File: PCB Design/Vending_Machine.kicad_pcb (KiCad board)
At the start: 2 copper layers, 113.8 x 144.3 mm, 126 parts, among them J1 Mains, J11 Conn_Sig, J12 Conn_Aux, J13 Conn_I2C, J15 Conn_I2C, J2 Conn_0-7, J3 Conn_8, J31 Conn_01x15, J32 Conn_01x15, J33 UART0, J34 UART2, J35 GPIO, J36 Display, J37 I2C, J38 I2C, J39 SPI, J4 Conn_9, J40 GPIO, SW31 EN, SW32 BOOT, U11 AMS1117-3.3, U12 SX1509BIULTRT, U13 TCA9406DC, U31 AMS1117-3.3, U32 ESP32-WROOM-32UE, U33 TCA9406DC

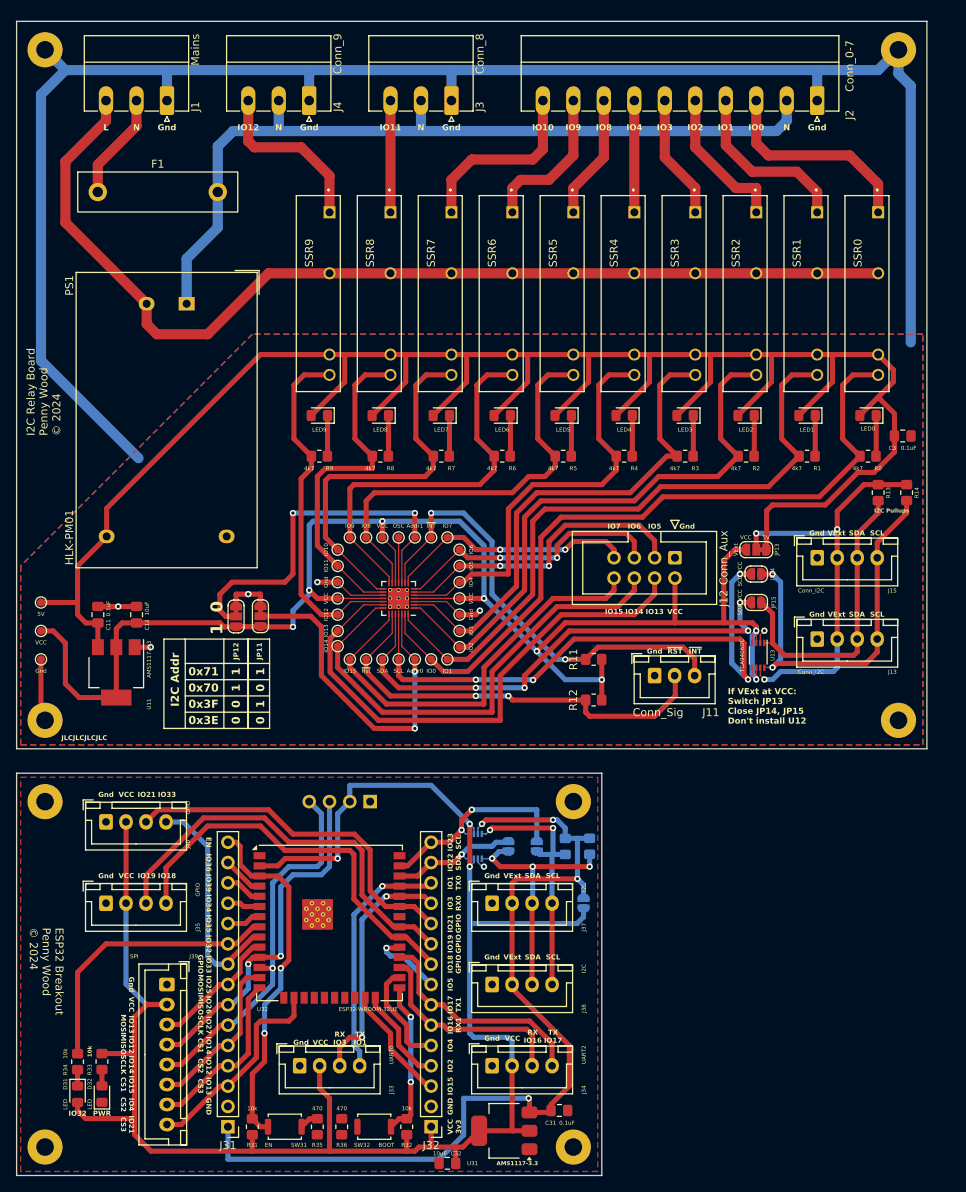
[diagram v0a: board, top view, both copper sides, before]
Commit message: Added Multiplexer
Added separate IO Multiplexer breakout
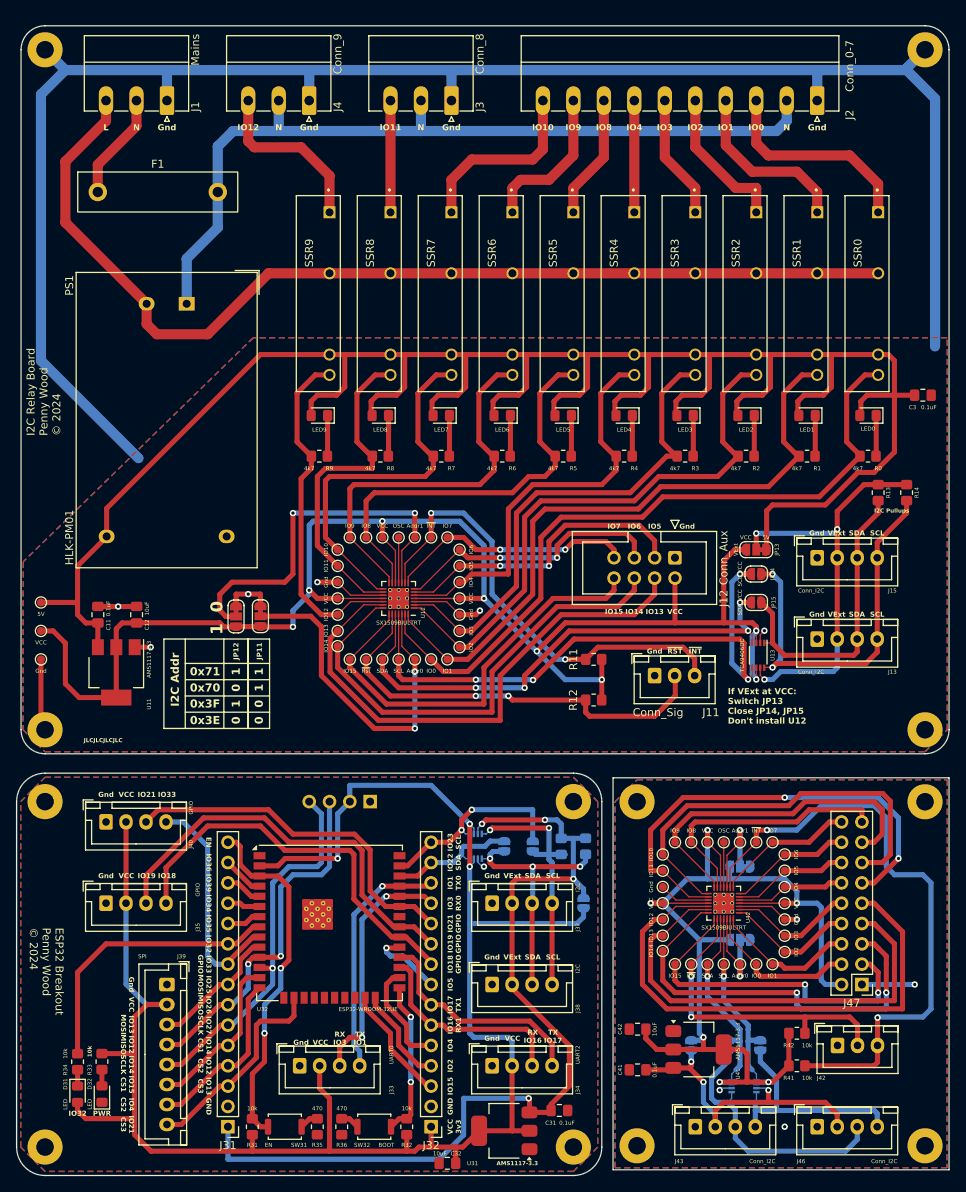
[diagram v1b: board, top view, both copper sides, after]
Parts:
- added Addr0: , Footprints:TestPoint_Pad_D1.0mm, F.Cu at (137.7, 165.1)
- added Addr1: , Footprints:TestPoint_Pad_D1.0mm, F.Cu at (137.7, 149.9)
- added C41: 0.1uF, Capacitor_SMD:C_0805_2012Metric_Pad1.18x1.45mm_HandSolder, F.Cu at (124.9, 178.3)
- added C42: 10uF, Capacitor_SMD:C_0805_2012Metric_Pad1.18x1.45mm_HandSolder, F.Cu at (124.9, 173.2)
- added Gnd: , Footprints:TestPoint_Pad_D1.0mm, F.Cu at (128.0, 155.4)
- added Gnd: , Footprints:TestPoint_Pad_D1.0mm, F.Cu at (143.3, 159.5)
- added H31: MountingHole_2.2mm_M2_Pad, MountingHole:MountingHole_2.2mm_M2_Pad, F.Cu at (160.8, 144.8)
- added H31: MountingHole_2.2mm_M2_Pad, MountingHole:MountingHole_2.2mm_M2_Pad, F.Cu at (124.8, 144.8)
- added H31: MountingHole_2.2mm_M2_Pad, MountingHole:MountingHole_2.2mm_M2_Pad, F.Cu at (160.8, 187.8)
- added H31: MountingHole_2.2mm_M2_Pad, MountingHole:MountingHole_2.2mm_M2_Pad, F.Cu at (124.8, 187.8)
- added IO0: , Footprints:TestPoint_Pad_D1.0mm, F.Cu at (139.7, 165.1)
- added IO1: , Footprints:TestPoint_Pad_D1.0mm, F.Cu at (141.7, 165.1)
- added IO10: , Footprints:TestPoint_Pad_D1.0mm, F.Cu at (128.0, 151.4)
- added IO11: , Footprints:TestPoint_Pad_D1.0mm, F.Cu at (128.0, 153.4)
- added IO12: , Footprints:TestPoint_Pad_D1.0mm, F.Cu at (128.0, 159.5)
- added IO13: , Footprints:TestPoint_Pad_D1.0mm, F.Cu at (128.0, 161.5)
- added IO14: , Footprints:TestPoint_Pad_D1.0mm, F.Cu at (128.0, 163.4)
- added IO15: , Footprints:TestPoint_Pad_D1.0mm, F.Cu at (129.5, 165.1)
- added IO2: , Footprints:TestPoint_Pad_D1.0mm, F.Cu at (143.3, 163.6)
- added IO3: , Footprints:TestPoint_Pad_D1.0mm, F.Cu at (143.3, 161.5)
- added IO4: , Footprints:TestPoint_Pad_D1.0mm, F.Cu at (143.3, 155.4)
- added IO5: , Footprints:TestPoint_Pad_D1.0mm, F.Cu at (143.3, 153.4)
- added IO6: , Footprints:TestPoint_Pad_D1.0mm, F.Cu at (143.3, 151.4)
- added IO7: , Footprints:TestPoint_Pad_D1.0mm, F.Cu at (141.7, 149.9)
- added IO8: , Footprints:TestPoint_Pad_D1.0mm, F.Cu at (131.6, 149.9)
- added IO9: , Footprints:TestPoint_Pad_D1.0mm, F.Cu at (129.5, 149.9)
- added J42: Conn_Sig, Connector_JST:JST_XH_B3B-XH-A_1x03_P2.50mm_Vertical, F.Cu at (149.9, 175.3)
- added J43: Conn_I2C, Connector_JST:JST_XH_B4B-XH-A_1x04_P2.50mm_Vertical, F.Cu at (132.1, 185.4)
- added J46: Conn_I2C, Connector_JST:JST_XH_B4B-XH-A_1x04_P2.50mm_Vertical, F.Cu at (147.3, 185.4)
- added J47: Conn, Connector_PinHeader_2.54mm:PinHeader_2x09_P2.54mm_Vertical, F.Cu at (152.9, 167.6)
- added JP41: ADDR0, Jumper:SolderJumper-3_P1.3mm_Bridged12_RoundedPad1.0x1.5mm_NumberLabels, B.Cu at (137.7, 162.1)
- added JP42: ADDR1, Jumper:SolderJumper-3_P1.3mm_Bridged12_RoundedPad1.0x1.5mm_NumberLabels, B.Cu at (137.7, 152.9)
- added JP43: SCL_VCC, Jumper:SolderJumper-2_P1.3mm_Open_RoundedPad1.0x1.5mm, B.Cu at (140.2, 175.3)
- added JP44: SDA_VCC, Jumper:SolderJumper-2_P1.3mm_Open_RoundedPad1.0x1.5mm, B.Cu at (136.1, 175.3)
- added JP45: VCC_VExt, Jumper:SolderJumper-2_P1.3mm_Open_RoundedPad1.0x1.5mm, B.Cu at (131.6, 175.3)
- added OSC: , Footprints:TestPoint_Pad_D1.0mm, F.Cu at (135.6, 149.9)
- added R41: 10k, Resistor_SMD:R_0805_2012Metric_Pad1.20x1.40mm_HandSolder, F.Cu at (144.8, 177.8)
- added R42: 10k, Resistor_SMD:R_0805_2012Metric_Pad1.20x1.40mm_HandSolder, F.Cu at (144.8, 173.7)
- added SCL: SCL_VCC, Footprints:TestPoint_Pad_D1.0mm, F.Cu at (135.6, 165.1)
- added SDA: , Footprints:TestPoint_Pad_D1.0mm, F.Cu at (133.6, 165.1)
- added U41: AMS1117-3.3, Package_TO_SOT_SMD:SOT-223-3_TabPin2, F.Cu at (132.5, 175.8)
- added U42: SX1509BIULTRT, Package_DFN_QFN:QFN-28-1EP_4x4mm_P0.4mm_EP2.6x2.6mm_ThermalVias, F.Cu at (135.6, 157.5)
- added U43: TCA9406DC, Package_SO:VSSOP-8_2.3x2mm_P0.5mm, B.Cu at (138.2, 180.3)
- added VCC: 4, Footprints:TestPoint_Pad_D1.0mm, F.Cu at (143.3, 157.5)
- added VCC: 12, Footprints:TestPoint_Pad_D1.0mm, F.Cu at (133.6, 149.9)
- added VCC: 18, Footprints:TestPoint_Pad_D1.0mm, F.Cu at (128.0, 157.5)
- added ~{INT}: , Footprints:TestPoint_Pad_D1.0mm, F.Cu at (139.7, 149.9)
- added ~{Rst}: , Footprints:TestPoint_Pad_D1.0mm, F.Cu at (131.6, 165.1)
- moved B2 72.3 mm to (51.6, 191.5), turned to 180 degrees
- moved B1 43.3 mm to (163.8, 127.1)
- moved C3 5.68 mm to (160.5, 94.0)
- moved H4 3.52 mm to (160.8, 135.8)
- moved H2 3.32 mm to (160.8, 50.8)
- moved H3 1.18 mm to (50.8, 135.8)
- moved JP32 0.51 mm to (108.2, 150.4)
- moved JP31 0.51 mm to (111.8, 150.4)
- moved R37 0.51 mm to (118.4, 150.4)
- moved R38 0.51 mm to (115.3, 150.4)
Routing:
- net /IO Multiplexer/VCC: track 0.00 -> 127.6 mm, vias 0 -> 6
- net /IO Multiplexer/~{INT}: track 0.00 -> 76.8 mm, vias 0 -> 2
- net /IO Multiplexer/IO12: track 0.00 -> 66.1 mm
- net /IO Multiplexer/IO11: track 0.00 -> 58.3 mm, vias 0 -> 2
- net /IO Multiplexer/IO13: track 0.00 -> 57.6 mm
- net /IO Multiplexer/IO10: track 0.00 -> 52.1 mm
- net /IO Multiplexer/IO14: track 0.00 -> 51.9 mm, vias 0 -> 2
- net /IO Multiplexer/IO15: track 0.00 -> 43.4 mm, vias 0 -> 2
- net /IO Multiplexer/IO9: track 0.00 -> 43.0 mm
- net /IO Multiplexer/VExt: track 0.00 -> 39.5 mm, vias 0 -> 3
- net /IO Multiplexer/~{RST}: track 0.00 -> 39.4 mm, vias 0 -> 2
- net /IO Multiplexer/SDA: track 0.00 -> 33.5 mm
- net /IO Multiplexer/IO8: track 0.00 -> 32.8 mm
- net /IO Multiplexer/SCL: track 0.00 -> 29.8 mm
- net /IO Multiplexer/SDA_VCC: track 0.00 -> 24.5 mm, vias 0 -> 1
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- added copper zone on B.Cu, net /IO Multiplexer/GND
- added copper zone on F.Cu, net /IO Multiplexer/GND
- added copper zone on B.Cu, net /Logic Controller/GND
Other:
- board size 113.8 x 144.3 mm -> 116.6 x 143.7 mm
- board text added: "JP41 ADDR0"
- board text added: "JP42 ADDR1"

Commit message: Minor Improvements
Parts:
- added B3: Multiplexer, PCM_kikit:Board, F.Cu at (139.3, 190.8)
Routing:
- net /IO Multiplexer/~{INT}: track 76.8 -> 70.8 mm
- net /IO Multiplexer/GND: track 22.4 -> 23.2 mm
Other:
- outline, holes or cut-outs redrawn

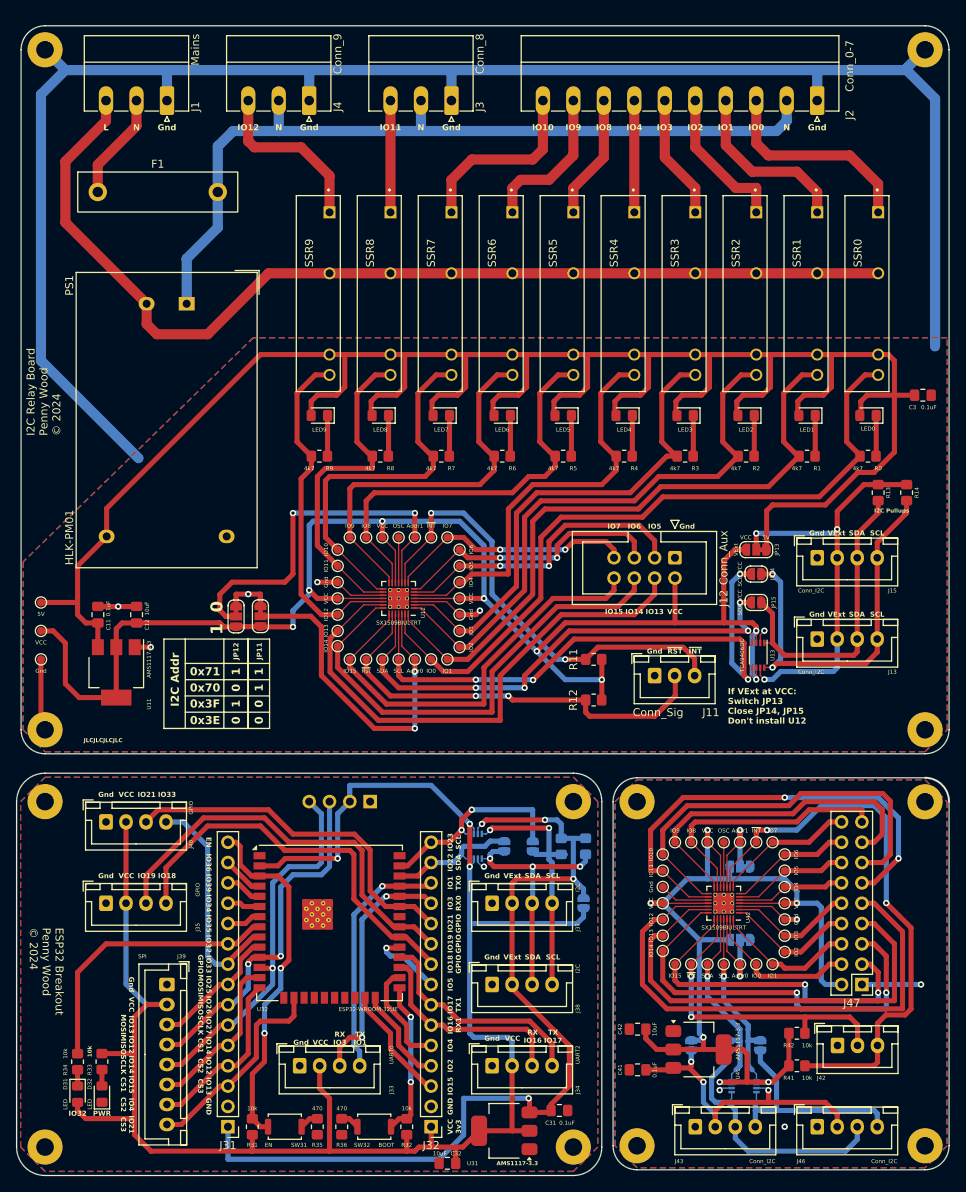
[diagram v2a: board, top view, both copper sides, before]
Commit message: Tweaks and Updates
Added OSCIO pin to breakout board.
A few more tweaks
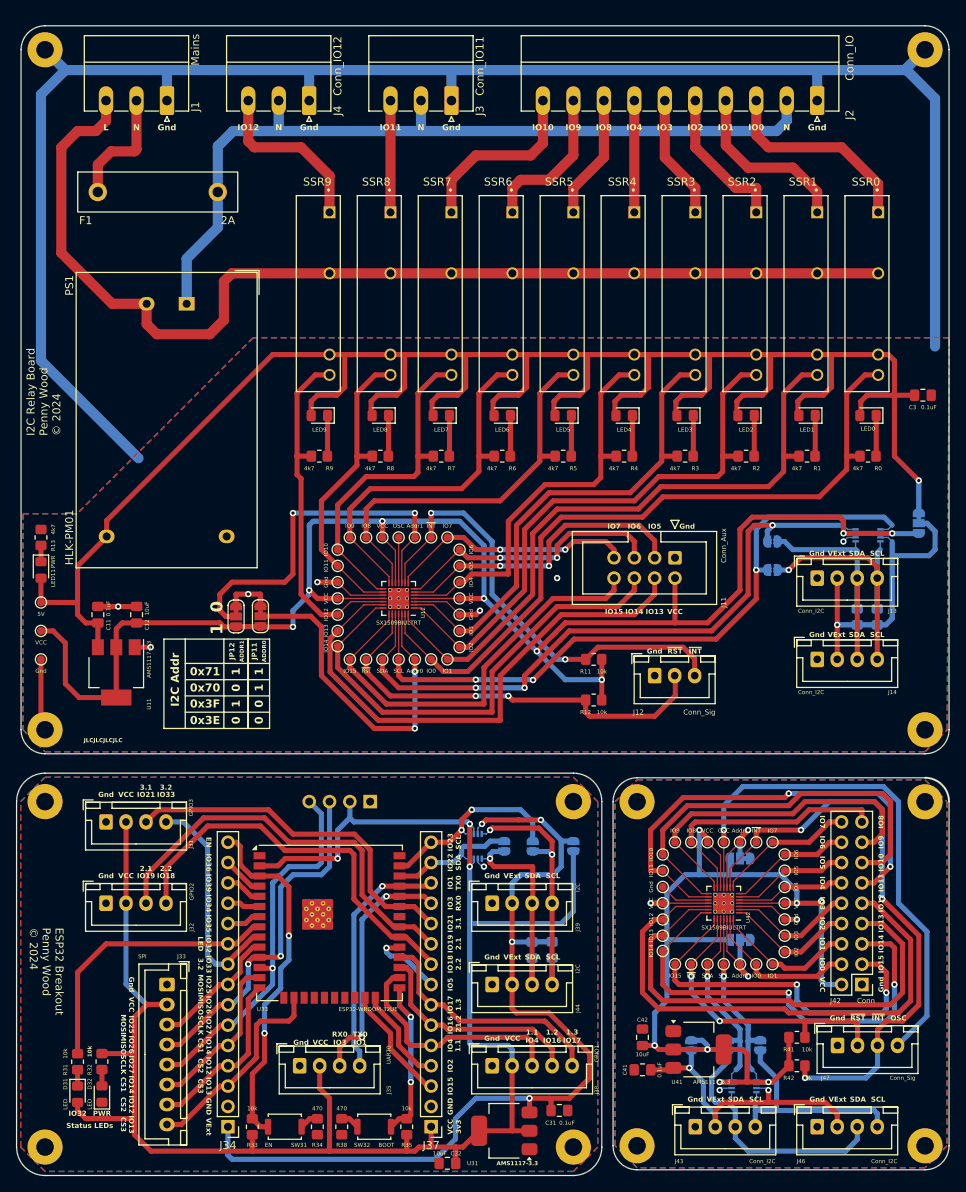
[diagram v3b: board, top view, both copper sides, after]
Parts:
- added LED11: PWR, LED_SMD:LED_0805_2012Metric_Pad1.15x1.40mm_HandSolder, F.Cu at (50.3, 115.8)
- added R13: 4k7, Resistor_SMD:R_0805_2012Metric_Pad1.20x1.40mm_HandSolder, F.Cu at (50.3, 111.8)
- J2: value Conn_0-7 -> Conn_IO
- J3: value Conn_8 -> Conn_IO11
- J31: renamed from J40; value GPIO -> GPIO3
- J32: renamed from J35; value GPIO -> GPIO2
- J38: renamed from J34; value UART2 -> GPIO1; footprint Connector_JST:JST_XH_B4B-XH-A_1x04_P2.50mm_Vertical -> Connector_JST:JST_XH_B5B-XH-A_1x05_P2.50mm_Vertical
- J4: value Conn_9 -> Conn_IO12
- J47: renamed from J42; footprint Connector_JST:JST_XH_B3B-XH-A_1x03_P2.50mm_Vertical -> Connector_JST:JST_XH_B4B-XH-A_1x04_P2.50mm_Vertical
- JP13, JP14, JP15, U13: moved to B.Cu
- R14: renamed from R13; moved to B.Cu
- R15: renamed from R14; moved to B.Cu
- moved JP13 20.6 mm to (160.0, 110.0), turned to -90 degrees
- moved U13 20.3 mm to (153.7, 111.5), turned to 0 degrees
- moved R15 16.0 mm to (154.8, 121.7), turned to 90 degrees
- moved R14 15.7 mm to (152.3, 121.7), turned to 90 degrees
- moved R36 14.6 mm to (111.7, 163.3)
- moved R37 13.0 mm to (114.2, 163.3)
- moved JP15 7.89 mm to (141.7, 112.3)
- moved JP33 7.22 mm to (116.8, 150.4)
- moved J13 2.54 mm to (147.3, 116.8)
- moved J14 2.54 mm to (147.3, 127.0)
- moved JP14 2.09 mm to (141.7, 115.8)
- moved C42 1.19 mm to (125.5, 174.2), turned to 90 degrees
- moved JP45 1.02 mm to (137.7, 151.9)
- moved C41 0.61 mm to (125.5, 178.3)
- moved R41 0.51 mm to (144.8, 174.2)
- renumbered J12 to J11, J11 to J12, J15 to J13, J13 to J14, J39 to J33, J31 to J34, J33 to J35, J32 to J37, J37 to J39, J47 to J42, J38 to J44, JP45 to JP41, JP43 to JP42, JP44 to JP43, JP41 to JP44, JP42 to JP45, R34 to R31, R33 to R32, R31 to R33, R35 to R34, R32 to R35, R37 to R36, R38 to R37, R36 to R38, R42 to R41, R41 to R42, U33 to U32, U32 to U33
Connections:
- J38 pad 3: /Logic Controller/IO16 -> /Logic Controller/IO4
- J38 pad 4: /Logic Controller/IO17 -> /Logic Controller/IO16
- OSC pad 11: unconnected-(U42-OSCIO-Pad11) -> /IO Multiplexer/OSCIO
- U42 pad 11: unconnected-(U42-OSCIO-Pad11) -> /IO Multiplexer/OSCIO
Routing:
- net /IO Multiplexer/OSCIO: track 0.00 -> 67.3 mm, vias 0 -> 1
- net /Relay Controller/SDA_VCC: track 65.4 -> 84.3 mm, vias 4 -> 3
- net /Logic Controller/IO4: track 13.4 -> 29.6 mm
- net /Relay Controller/SCL: track 49.3 -> 33.7 mm, vias 2 -> 1
- net /Relay Controller/VExt: track 53.2 -> 39.1 mm, vias 3 -> 1
- net /Relay Controller/VCC: track 197.2 -> 210.9 mm
- net /Relay Controller/+5V: track 273.2 -> 260.3 mm, vias 0 -> 1
- net /Relay Controller/SCL_VCC: track 75.7 -> 86.7 mm, vias 4 -> 3
- net /Relay Controller/SDA: track 38.1 -> 28.8 mm
- net /IO Multiplexer/GND: track 23.2 -> 15.8 mm, vias 4 -> 2
- net /Relay Controller/Live: track 129.4 -> 136.5 mm
- net unconnected-(U42-OSCIO-Pad11): track 5.68 -> 0.00 mm
- net /IO Multiplexer/IO14: track 51.9 -> 56.4 mm
- net /Logic Controller/SDA: track 32.0 -> 27.6 mm, vias 3 -> 1
- net /Relay Controller/IO10: track 46.2 -> 41.9 mm
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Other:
- board text added: "1.1"
- board text added: "1.2"
- board text added: "1.3"
- board text added: "2.1"
- board text added: "2.2"
- board text added: "21.2"
- board text added: "3.1"
- board text added: "3.2"
- board text added: "ADDR0"
- board text added: "ADDR1"
- board text added: "If VExt at VCC: Switch JP13 Close JP14, JP15 Don't install U13"
- board text added: "If VExt powers VCC: Also don't install U11"
- board text added: "If power on VExt @ 3v3: Close JP43, JP44, JP45 Don't install U41, U43"
- board text added: "Install I2C Pullups In one location On the bus"
- board text added: "Install I2C pullups in one location On the bus"
- board text added: "LED"
- board text added: "OSC"
- board text added: "Status LEDs"
- board text removed: "GPIO"
- board text removed: "If VExt at VCC: Switch JP13 Close JP14, JP15 Don't install U12"
- board text removed: "RX"
- board text removed: "RX1"
- board text removed: "TX"
- board text removed: "TX1"
